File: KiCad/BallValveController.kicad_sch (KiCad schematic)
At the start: 46 parts, among them J1 Screw_Terminal_01x03, J10 Screw_Terminal_01x04, J11 Screw_Terminal_01x02, J2 Screw_Terminal_01x04, J3 Screw_Terminal_01x04, J4 Screw_Terminal_01x04, J5 Conn_01x01_Male, J6 Conn_01x01_Male, J7 Conn_01x01_Male, J8 Conn_01x01_Male, J9 Conn_01x01_Male, K1 G5V-2, Q1 Q_PMOS_GDS, Q2 2N2222A, U1 L7805, U2 SeedStudio XIAO ESP32 C3 v1

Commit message: v7.0.1 - updated metadata only
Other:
- note added: "GPIO2 - /BAT READ GPIO3/A1 - BAT Vin GPIO4 - /VOPEN GPIO5 - /VCLOSE GPIO6 - I2C SDA GPIO7 - I2C SCL GPIO8 - NC GPIO9 - ILED GPIO10 - VALVE GPIO20 - RX / 1-wire GPIO21 - TX / 1-wire"
- note removed: "GPIO2 - /BAT READ GPIO3/A1 - BAT Vin GPIO4 - /VOPEN GPIO5 - /VCLOSE GPIO6 - I2C SDA GPIO7 - I2C SCL GPIO8 - NC GPIO9 - ILED GPIO10 - VALVE GPIO21 - TX / 1-wire GPIO21 - RX / 1-wire"

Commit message: First ESP32C6 layout
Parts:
- removed U2: SeedStudio XIAO ESP32 C3 v1, LOCAL1:XIAO_ESP32C3_THT, symbol LOCAL1:XIAO_ESP32C3_THT
- added JP4: SolderJumper_2_Open, Jumper:SolderJumper-2_P1.3mm_Open_RoundedPad1.0x1.5mm, symbol Jumper:SolderJumper_2_Open
- added U3: XIAO-ESP32-C6, LOCAL1:XIAO-ESP32-C6-SMD, symbol LOCAL1:XIAO-ESP32-C6-SMD
- C2, C3, C4: footprint Capacitor_Tantalum_SMD:CP_EIA-3216-18_Kemet-A_Pad1.58x1.35mm_HandSolder -> Capacitor_SMD:C_1206_3216Metric_Pad1.33x1.80mm_HandSolder
- J10, J2, J3, J4: symbol Connector:Screw_Terminal_01x04 -> Connector:Conn_01x04_Pin
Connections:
- net +3V3: now also U3.12 (3V3)
- net +5V: now also U3.14 (5V)
- net GND: now also U3.13 (GND), U3.16 (GND), U3.20 (GND)
- net PwrIn: now also JP4.1 (A)
- net SCL: now also U3.6 (GPIO23_D5_SCL)
- net SDA: now also U3.5 (GPIO22_D4_SDA)
- net TX: now also U3.7 (GPIO16_D6_TX)
- net VBAT: now also U3.15 (BAT)
- net VCLOSE: now also U3.4 (GPIO21_D3)
- net VOPEN: now also U3.3 (GPIO2_A2_D2)
- net Vimplant: now also JP4.2 (B)
- net at C1.1, R3.2: now also U3.1 (GPIO0_A0_D0)
- net at D2.2 (A), R10.2: now also U3.8 (GPIO17_D7_RX)
- net at R11.1: now also U3.10 (GPIO20_D9_MISO)
- net at D5.2 (A): now also U3.11 (GPIO18_D10_MOSI)
- net at R1.2, R2.1: now also U3.2 (GPIO1_A1_D1)
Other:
- note added: "GPIO0/D0 - /BAT READ GPIO1/A1 - BAT Vin GPIO2/D2 - /VOPEN GPIO21/D3 - /VCLOSE GPIO22/D4 - I2C SDA GPIO23/D5 - I2C SCL GPIO20/D9 - ILED GPIO18/D10 - VALVE GPIO17/D7 - RX / 1-wire GPIO16/D6 - TX / 1-wire"
- note removed: "GPIO2 - /BAT READ GPIO3/A1 - BAT Vin GPIO4 - /VOPEN GPIO5 - /VCLOSE GPIO6 - I2C SDA GPIO7 - I2C SCL GPIO8 - NC GPIO9 - ILED GPIO10 - VALVE GPIO20 - RX / 1-wire GPIO21 - TX / 1-wire"
- moved on the sheet: D1, D2, JP1, R10, R9

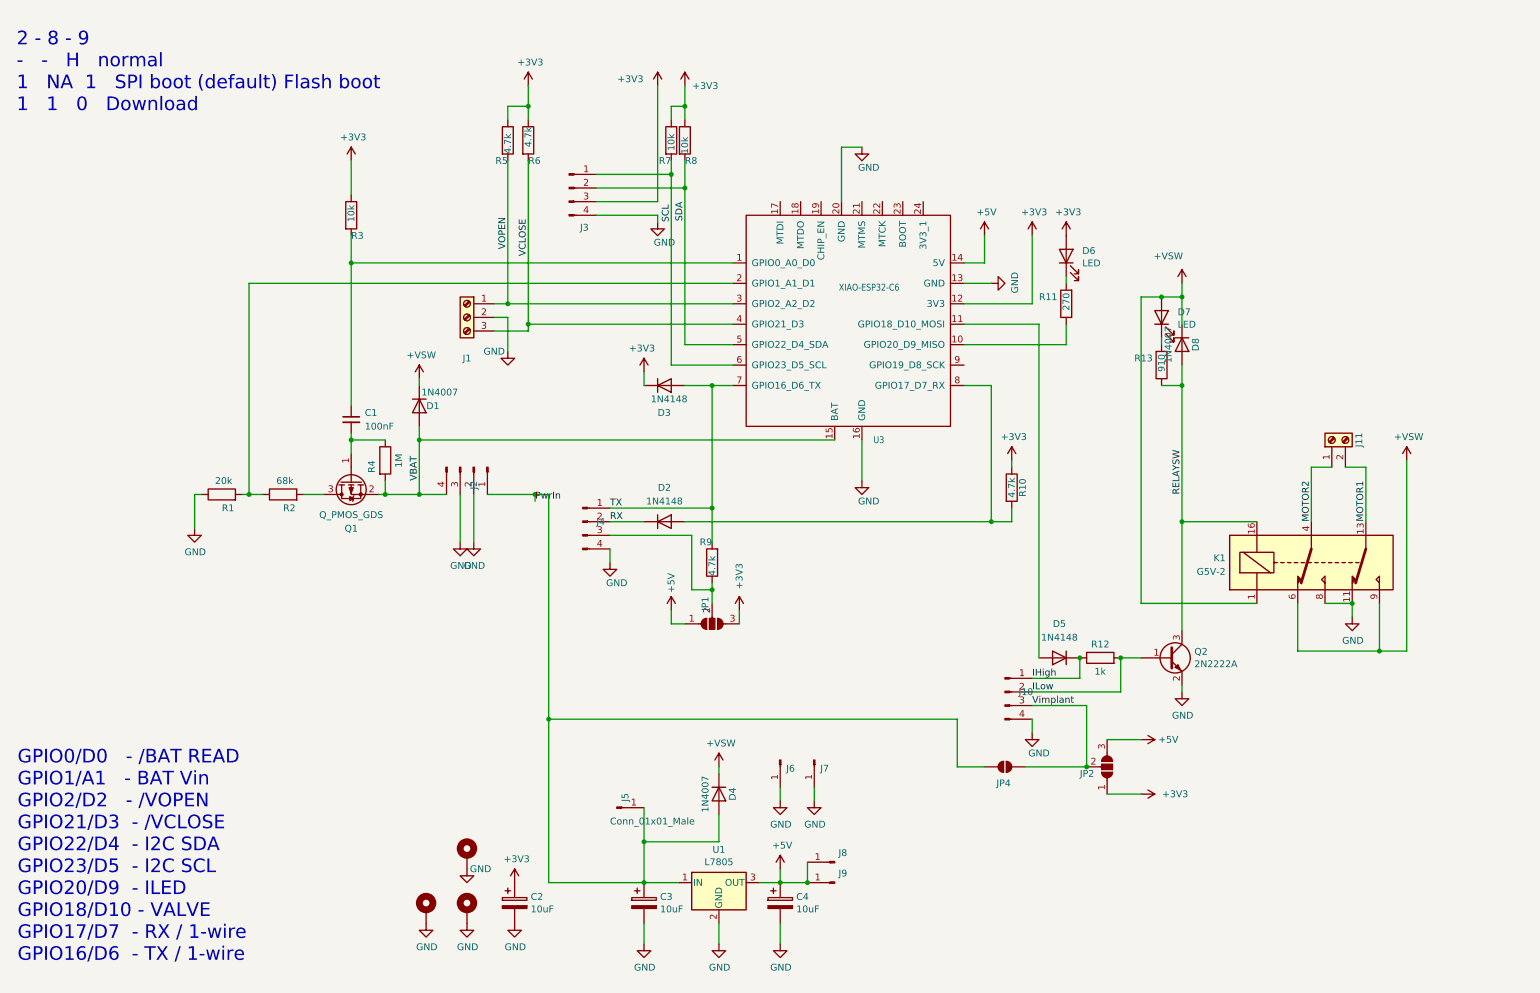
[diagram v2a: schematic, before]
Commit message: Added step down converter
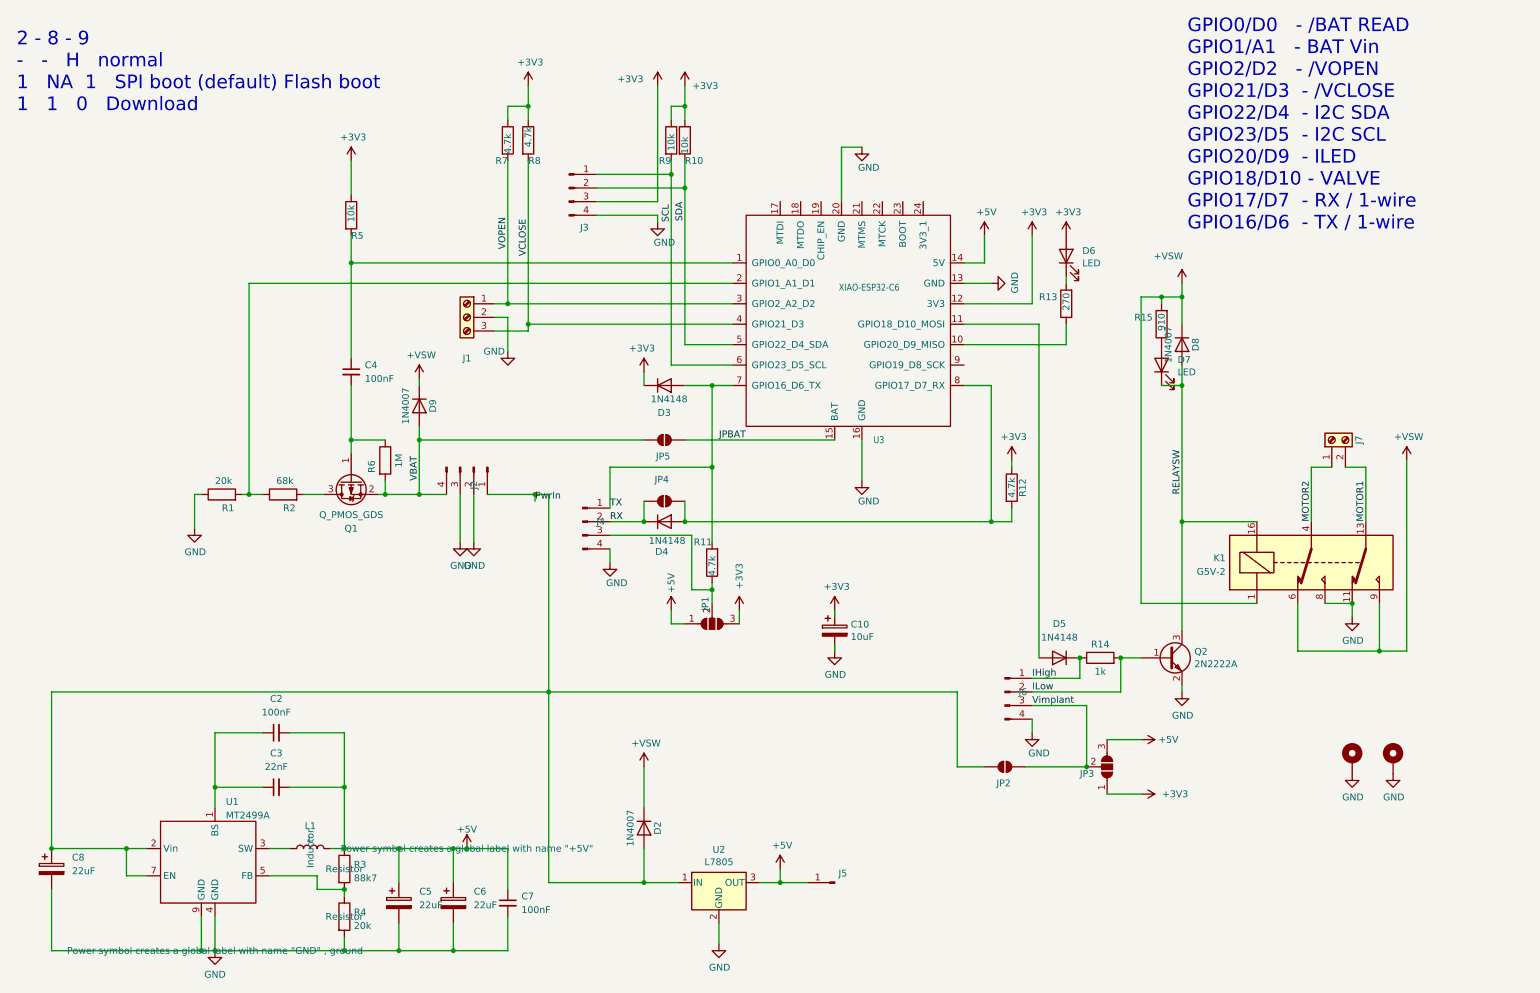
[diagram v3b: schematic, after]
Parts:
- removed C3, C4: 10uF, Capacitor_SMD:C_1206_3216Metric_Pad1.33x1.80mm_HandSolder, symbol Device:CP
- removed D1: 1N4007, Diode_SMD:D_SMB_Handsoldering, symbol Diode:1N4007
- removed H3: MountingHole_Pad, MountingHole:MountingHole_3.2mm_M3_ISO14580_Pad, symbol Mechanical:MountingHole_Pad
- removed J5, J6, J7, J9: Conn_01x01_Male, Connector_PinHeader_2.54mm:PinHeader_1x01_P2.54mm_Vertical, symbol Connector:Conn_01x01_Male
- added C2, C7: 100nF, Capacitor_SMD:C_0805_2012Metric_Pad1.18x1.45mm_HandSolder, symbol Device:C_Small
- added C3: 22nF, Capacitor_SMD:C_0805_2012Metric_Pad1.18x1.45mm_HandSolder, symbol Device:C_Small
- added C5, C6, C8: 22uF, Capacitor_SMD:C_1206_3216Metric_Pad1.33x1.80mm_HandSolder, symbol Device:C_Polarized
- added D9: 1N4007, Diode_SMD:D_SMB_Handsoldering, symbol Diode:1N4007
- added JP4, JP5: SolderJumper_2_Open, Jumper:SolderJumper-2_P1.3mm_Open_RoundedPad1.0x1.5mm, symbol Jumper:SolderJumper_2_Open
- added L1: L, Inductor_SMD:L_Bourns-SRU8028_8.0x8.0mm, symbol Device:L
- added R3: 88k7, Resistor_SMD:R_0805_2012Metric_Pad1.20x1.40mm_HandSolder, symbol Device:R
- added R4: 20k, Resistor_SMD:R_0805_2012Metric_Pad1.20x1.40mm_HandSolder, symbol Device:R
- added U1: MT2499A, Package_SO:TI_SO-PowerPAD-8, symbol custom_kicad_lib_sk:MT499A
- C10: renamed from C2; symbol Device:CP -> Device:C_Polarized
- D3, D5: symbol Diode:1N4148 -> Device:D
- D4: renamed from D2; symbol Diode:1N4148 -> Device:D
- Q1: footprint Package_TO_SOT_SMD:SOT-23_Handsoldering -> Package_TO_SOT_SMD:SOT-23
- renumbered C1 to C4, D4 to D2, H4 to H3, J8 to J5, J10 to J6, J11 to J7, JP4 to JP2, JP2 to JP3, R8 to R10, R9 to R11, R10 to R12, R11 to R13, R12 to R14, R13 to R15, R3 to R5, R4 to R6, R5 to R7, R6 to R8, R7 to R9, U1 to U2
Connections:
- net +5V: now also C2.2, C3.2, C5.1, C6.1, C7.1, L1.2, R3.1
- net +VSW: now also R15.2, D9.1 (K); no longer D7.2 (A)
- net GND: now also C5.2, C6.2, C7.2, C8.2, R4.2, U1.4 (GND), U1.9 (GND)
- net PwrIn: now also C8.1, U1.2 (Vin), U1.7 (EN)
- net RELAYSW: now also D7.1 (K); no longer R15.1
- net RX: now also JP4.1 (A)
- net VBAT: now also D9.2 (A), JP5.1 (A); no longer U3.15 (BAT)
- net at D4.2 (A), R12.2, U3.8 (GPIO17_D7_RX): now also JP4.2 (B)
- new net: D7.2 (A), R15.1
- new net: R3.2, R4.1, U1.5 (FB)
- new net: C2.1, C3.1, U1.1 (BS)
- new net: L1.1, U1.3 (SW)
- new net JPBAT: JP5.2 (B), U3.15 (BAT)
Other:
- moved on the sheet: C10, C4, D2, D7, J5, R15

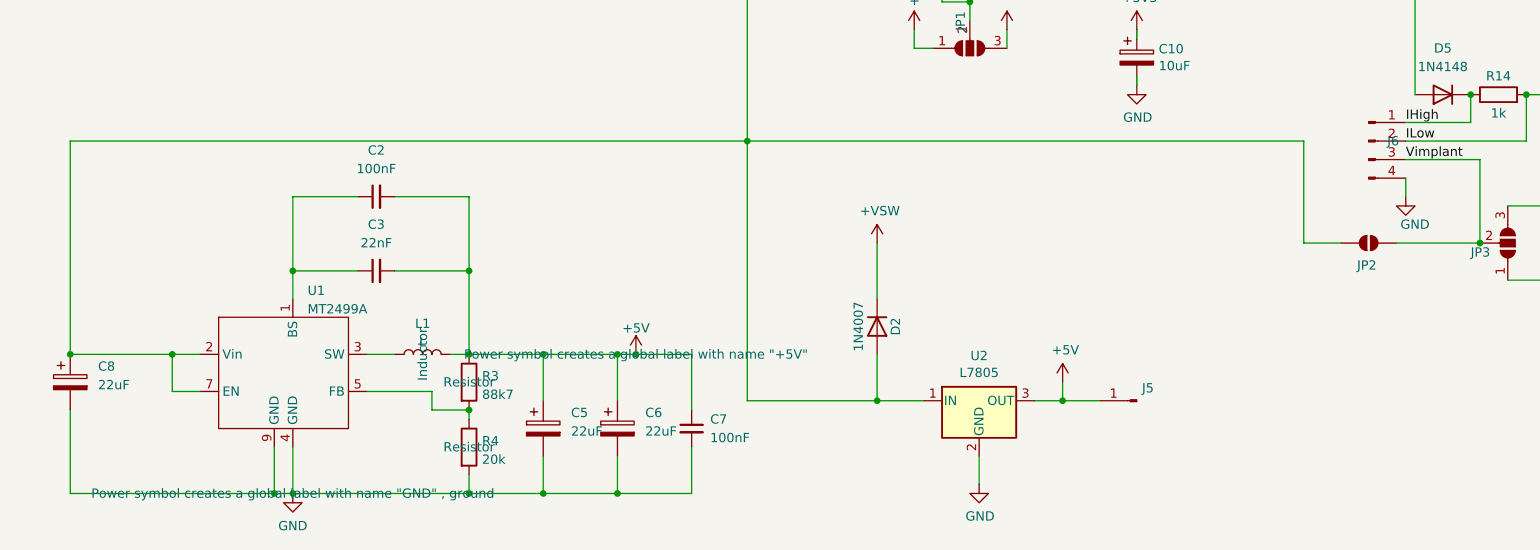
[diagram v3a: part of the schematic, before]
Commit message: New diode footprints
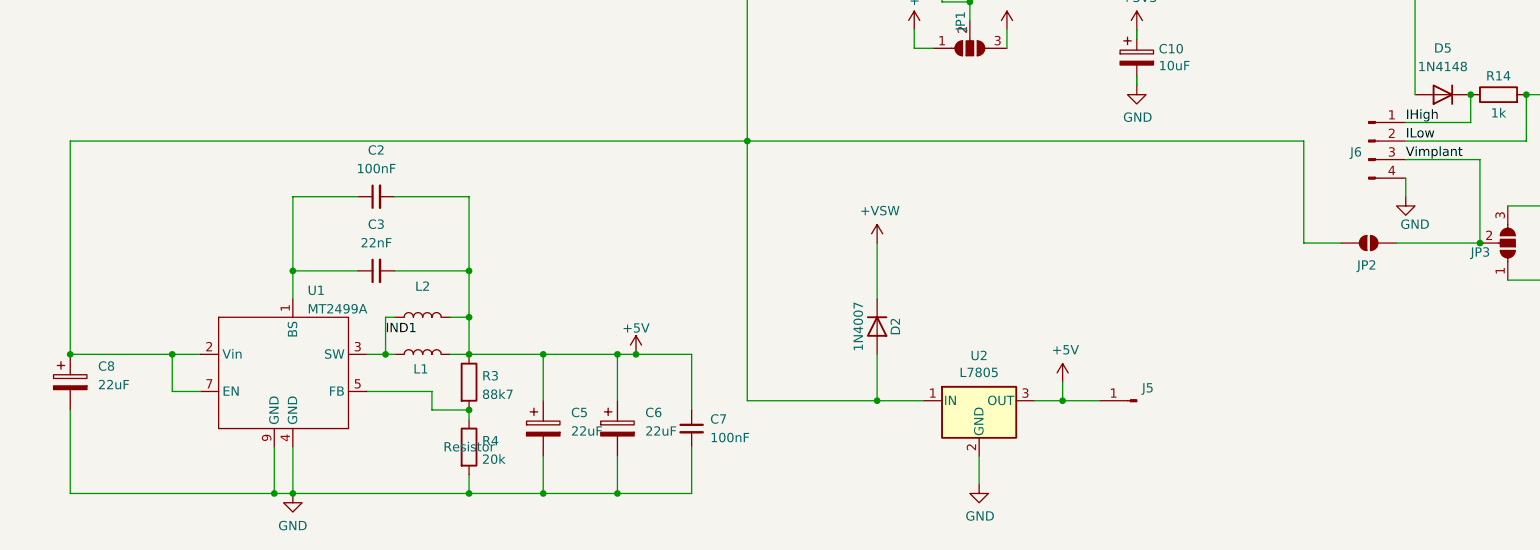
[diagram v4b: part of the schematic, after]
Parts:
- added L2: L, Inductor_SMD:L_Bourns-SRU8028_8.0x8.0mm, symbol Device:L
- D2, D8, D9: footprint Diode_SMD:D_SMB_Handsoldering -> Diode_SMD:D_SOD-123
- D3, D4, D5: footprint Diode_SMD:D_MiniMELF -> Diode_SMD:D_SOD-123
- L1: footprint Inductor_SMD:L_Bourns-SRU8028_8.0x8.0mm -> Inductor_SMD:L_2512_6332Metric_Pad1.52x3.35mm_HandSolder
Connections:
- net +5V: now also L2.2
- net IND1: now reaches L1.1, U1.3 (SW)
- net IND1: now also L2.1
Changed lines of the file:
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@@
 	)
 	(junction
+		(at 64.77 170.18)
+		(diameter 0)
+		(color 0 0 0 0)
+	)
+	(junction
 		(at 49.53 189.23)
 		(diameter 0)
@@
 	)
 	(junction
+		(at 76.2 165.1)
+		(diameter 0)
+		(color 0 0 0 0)
+	)
+	(junction
 		(at 58.42 104.14)
 		(diameter 0)
@@
 	(wire
 		(pts
-			(xy 52.07 189.23) (xy 52.07 182.88)
+			(xy 66.04 165.1) (xy 64.77 165.1)
 		)
 		(stroke
@@
 	(wire
 		(pts
-			(xy 96.52 170.18) (xy 99.06 170.18)
+			(xy 52.07 189.23) (xy 52.07 182.88)
 		)
 		(stroke
@@
 	(wire
 		(pts
-			(xy 62.23 170.18) (xy 66.04 170.18)
+			(xy 96.52 170.18) (xy 99.06 170.18)
 		)
 		(stroke
@@
 	(wire
 		(pts
+			(xy 62.23 170.18) (xy 64.77 170.18)
+		)
+		(stroke
+			(width 0)
+			(type default)
+		)
+	)
+	(wire
+		(pts
+			(xy 76.2 165.1) (xy 76.2 170.18)
+		)
+		(stroke
+			(width 0)
+			(type default)
+		)
+	)
+	(wire
+		(pts
 			(xy 200.66 106.68) (xy 200.66 109.22)
 		)
@@
 	(wire
 		(pts
-			(xy 76.2 158.75) (xy 76.2 170.18)
+			(xy 76.2 158.75) (xy 76.2 165.1)
 		)
 		(stroke
@@
 	(wire
 		(pts
+			(xy 64.77 170.18) (xy 66.04 170.18)
+		)
+		(stroke
+			(width 0)
+			(type default)
+		)
+	)
+	(wire
+		(pts
 			(xy 86.36 184.15) (xy 86.36 189.23)
 		)
@@
 	(wire
 		(pts
+			(xy 64.77 165.1) (xy 64.77 170.18)
+		)
+		(stroke
+			(width 0)
+			(type default)
+		)
+	)
+	(wire
+		(pts
 			(xy 168.91 39.37) (xy 172.72 39.37)
 		)
@@
 	(wire
 		(pts
+			(xy 73.66 165.1) (xy 76.2 165.1)
+		)
+		(stroke
+			(width 0)
+			(type default)
+		)
+	)
+	(wire
+		(pts
 			(xy 106.68 41.91) (xy 106.68 68.58)
 		)
@@
 		)
 	)
+	(label "IND1"
+		(at 64.77 167.64 0)
+		(effects
+			(font
+				(size 1.27 1.27)
+			)
+			(justify left bottom)
+		)
+	)
 	(label "SCL"
 		(at 137.16 53.34 90)
@@
 					(size 1.27 1.27)
 				)
+				(hide yes)
 			)
 		)
@@
 		(dnp no)
 		(property "Reference" "J6"
-			(at 201.93 140.97 0)
+			(at 196.85 142.494 0)
 			(effects
 				(font
@@
 			)
 		)
-		(property "Footprint" "Diode_SMD:D_MiniMELF"
+		(property "Footprint" "Diode_SMD:D_SOD-123"
 			(at 135.89 109.22 0)
 			(effects
@@
 			)
 		)
-		(property "Footprint" "Diode_SMD:D_SMB_Handsoldering"
+		(property "Footprint" "Diode_SMD:D_SOD-123"
 			(at 85.725 87.63 0)
 			(effects
@@
 					(size 1.27 1.27)
 				)
+				(hide yes)
 			)
 		)
@@
 			)
 		)
-		(property "Footprint" "Diode_SMD:D_MiniMELF"
+		(property "Footprint" "Diode_SMD:D_SOD-123"
 			(at 135.89 83.82 0)
 			(effects
@@
 					(size 1.27 1.27)
 				)
+				(hide yes)
 			)
 		)
@@
 		(on_board yes)
 		(dnp no)
-		(fields_autoplaced yes)
 		(property "Reference" "L1"
-			(at 69.85 165.9722 90)
+			(at 69.596 172.212 90)
 			(effects
 				(font
@@
 					(size 1.27 1.27)
 				)
+				(hide yes)
 			)
 		)
-		(property "Footprint" "Inductor_SMD:L_Bourns-SRU8028_8.0x8.0mm"
+		(property "Footprint" "Inductor_SMD:L_2512_6332Metric_Pad1.52x3.35mm_HandSolder"
 			(at 69.85 170.18 0)
 			(effects
@@
 					(size 1.27 1.27)
 				)
+				(hide yes)
 			)
 		)
@@
 	)
 	(symbol
+		(lib_id "Device:L")
+		(at 69.85 165.1 90)
+		(unit 1)
+		(exclude_from_sim no)
+		(in_bom yes)
+		(on_board yes)
+		(dnp no)
+		(fields_autoplaced yes)
+		(property "Reference" "L2"
+			(at 69.85 160.8922 90)
+			(effects
+				(font
+					(size 1.27 1.27)
+				)
+			)
+		)
+		(property "Value" "L"
+			(at 69.85 163.4291 90)
+			(effects
+				(font
+					(size 1.27 1.27)
+				)
+				(hide yes)
+			)
+		)
+		(property "Footprint" "Inductor_SMD:L_Bourns-SRU8028_8.0x8.0mm"
+			(at 69.85 165.1 0)
+			(effects
+				(font
+					(size 1.27 1.27)
+				)
+				(hide yes)
+			)
+		)
+		(property "Datasheet" "~"
+			(at 69.85 165.1 0)
+			(effects
+				(font
+					(size 1.27 1.27)
+				)
+				(hide yes)
+			)
+		)
+		(property "Description" "Inductor"
+			(at 69.85 165.1 0)
+			(effects
+				(font
+					(size 1.27 1.27)
+				)
+				(hide yes)
+			)
+		)
+		(property "JLCPCB Part#" "C2929438"
+			(at 69.85 165.1 90)
+			(effects
+				(font
+					(size 1.27 1.27)
+				)
+				(hide yes)
+			)
+		)
+		(pin "1"
+		)
+		(pin "2"
+		)
+		(instances
+			(project "BallValveController"
+				(path "/2a5b3e3c-2022-46db-8938-2c3b2e9edb6d"
+					(reference "L2")
+					(unit 1)
+				)
+			)
+		)
+	)
+	(symbol
 		(lib_id "power:GND")
 		(at 167.64 133.35 0)
@@
 			)
 		)
-		(property "Footprint" "Diode_SMD:D_MiniMELF"
+		(property "Footprint" "Diode_SMD:D_SOD-123"
 			(at 209.55 134.62 0)
 			(effects
@@
 					(size 1.27 1.27)
 				)
+				(hide yes)
 			)
 		)
@@
 			)
 		)
-		(property "Footprint" "Diode_SMD:D_SMB_Handsoldering"
+		(property "Footprint" "Diode_SMD:D_SOD-123"
 			(at 127.635 166.37 0)
 			(effects
@@
 			)
 		)
-		(property "Footprint" "Diode_SMD:D_SMB_Handsoldering"
+		(property "Footprint" "Diode_SMD:D_SOD-123"
 			(at 227.965 76.2 0)
 			(effects

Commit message: Footprint change 1N4148 to SOD-323
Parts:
- D3, D4, D5: footprint Diode_SMD:D_SOD-123 -> Diode_SMD:D_SOD-323_HandSoldering
- U3: footprint LOCAL1:XIAO-ESP32-C6-SMD -> LOCAL1:XIAO-ESP32-C3C6-SMD
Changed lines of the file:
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@@
 			)
 		)
-		(property "Footprint" "Diode_SMD:D_SOD-123"
+		(property "Footprint" "Diode_SMD:D_SOD-323_HandSoldering"
 			(at 135.89 109.22 0)
 			(effects
@@
 			)
 		)
-		(property "Footprint" "Diode_SMD:D_SOD-123"
+		(property "Footprint" "Diode_SMD:D_SOD-323_HandSoldering"
 			(at 135.89 83.82 0)
 			(effects
@@
 			)
 		)
-		(property "Footprint" "LOCAL1:XIAO-ESP32-C6-SMD"
+		(property "Footprint" "LOCAL1:XIAO-ESP32-C3C6-SMD"
 			(at 161.29 67.31 0)
 			(effects
@@
 			)
 		)
-		(property "Footprint" "Diode_SMD:D_SOD-123"
+		(property "Footprint" "Diode_SMD:D_SOD-323_HandSoldering"
 			(at 209.55 134.62 0)
 			(effects
